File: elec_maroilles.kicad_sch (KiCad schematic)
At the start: 14 parts

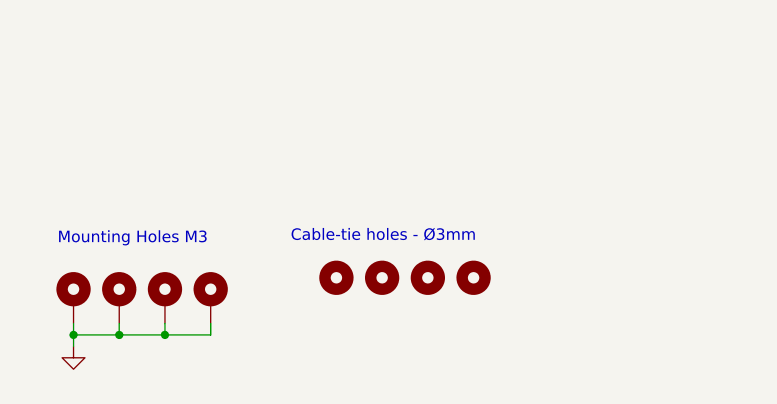
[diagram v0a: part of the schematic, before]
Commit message: [update] Better positionning.
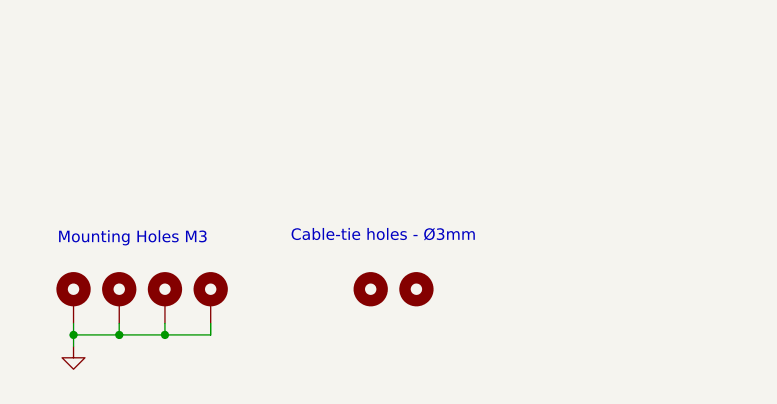
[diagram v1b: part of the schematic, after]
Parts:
- removed H12, H13: MountingHole_Pad, MountingHole:MountingHole_3.2mm_M3, symbol Mechanical:MountingHole
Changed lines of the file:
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@@
-	)
-	(symbol
-		(lib_id "Mechanical:MountingHole")
-		(at 146.05 170.18 0)
-		(unit 1)
-		(exclude_from_sim no)
-		(in_bom no)
-		(on_board yes)
-		(dnp no)
-		(property "Reference" "H13"
-			(at 148.59 168.91 0)
-			(effects
-				(font
-					(size 1.27 1.27)
-				)
-				(justify left)
-				(hide yes)
-			)
-		)
-		(property "Value" "MountingHole_Pad"
-			(at 152.4 163.83 0)
-			(effects
-				(font
-					(size 1.27 1.27)
-				)
-				(justify left)
-				(hide yes)
-			)
-		)
-		(property "Footprint" "MountingHole:MountingHole_3.2mm_M3"
-			(at 146.05 170.18 0)
-			(effects
-				(font
-					(size 1.27 1.27)
-				)
-				(hide yes)
-			)
-		)
-		(property "Datasheet" "~"
-			(at 146.05 170.18 0)
-			(effects
-				(font
-					(size 1.27 1.27)
-				)
-				(hide yes)
-			)
-		)
-		(property "Description" "Mounting Hole without connection"
-			(at 146.05 170.18 0)
-			(effects
-				(font
-					(size 1.27 1.27)
-				)
-				(hide yes)
-			)
-		)
-		(instances
-			(project "elec_zuuu_up"
-				(path "/bc05f5da-608c-4912-90e4-36b13d989976"
-					(reference "H13")
-					(unit 1)
-				)
-			)
-		)
 	)
 	(symbol
@@
 	(symbol
 		(lib_id "Mechanical:MountingHole")
-		(at 135.89 170.18 0)
+		(at 139.7 171.45 0)
 		(unit 1)
 		(exclude_from_sim no)
@@
 		(dnp no)
 		(property "Reference" "H11"
-			(at 138.43 168.91 0)
+			(at 142.24 170.18 0)
 			(effects
 				(font
@@
 		)
 		(property "Value" "MountingHole_Pad"
-			(at 142.24 163.83 0)
+			(at 146.05 165.1 0)
 			(effects
 				(font
@@
 		)
 		(property "Footprint" "MountingHole:MountingHole_3.2mm_M3"
-			(at 135.89 170.18 0)
-			(effects
-				(font
-					(size 1.27 1.27)
-				)
-				(hide yes)
-			)
-		)
-		(property "Datasheet" "~"
-			(at 135.89 170.18 0)
+			(at 139.7 171.45 0)
+			(effects
+				(font
+					(size 1.27 1.27)
+				)
+				(hide yes)
+			)
+		)
+		(property "Datasheet" "~"
+			(at 139.7 171.45 0)
 			(effects
 				(font
@@
 		)
 		(property "Description" "Mounting Hole without connection"
-			(at 135.89 170.18 0)
+			(at 139.7 171.45 0)
 			(effects
 				(font
@@
 				(path "/bc05f5da-608c-4912-90e4-36b13d989976"
 					(reference "FID1")
-					(unit 1)
-				)
-			)
-		)
-	)
-	(symbol
-		(lib_id "Mechanical:MountingHole")
-		(at 140.97 170.18 0)
-		(unit 1)
-		(exclude_from_sim no)
-		(in_bom no)
-		(on_board yes)
-		(dnp no)
-		(property "Reference" "H12"
-			(at 143.51 168.91 0)
-			(effects
-				(font
-					(size 1.27 1.27)
-				)
-				(justify left)
-				(hide yes)
-			)
-		)
-		(property "Value" "MountingHole_Pad"
-			(at 147.32 163.83 0)
-			(effects
-				(font
-					(size 1.27 1.27)
-				)
-				(justify left)
-				(hide yes)
-			)
-		)
-		(property "Footprint" "MountingHole:MountingHole_3.2mm_M3"
-			(at 140.97 170.18 0)
-			(effects
-				(font
-					(size 1.27 1.27)
-				)
-				(hide yes)
-			)
-		)
-		(property "Datasheet" "~"
-			(at 140.97 170.18 0)
-			(effects
-				(font
-					(size 1.27 1.27)
-				)
-				(hide yes)
-			)
-		)
-		(property "Description" "Mounting Hole without connection"
-			(at 140.97 170.18 0)
-			(effects
-				(font
-					(size 1.27 1.27)
-				)
-				(hide yes)
-			)
-		)
-		(instances
-			(project "elec_zuuu_up"
-				(path "/bc05f5da-608c-4912-90e4-36b13d989976"
-					(reference "H12")
 					(unit 1)
 				)
@@
 	(symbol
 		(lib_id "Mechanical:MountingHole")
-		(at 130.81 170.18 0)
+		(at 134.62 171.45 0)
 		(unit 1)
 		(exclude_from_sim no)
@@
 		(dnp no)
 		(property "Reference" "H10"
-			(at 133.35 168.91 0)
+			(at 137.16 170.18 0)
 			(effects
 				(font
@@
 		)
 		(property "Value" "MountingHole_Pad"
-			(at 137.16 163.83 0)
+			(at 140.97 165.1 0)
 			(effects
 				(font
@@
 		)
 		(property "Footprint" "MountingHole:MountingHole_3.2mm_M3"
-			(at 130.81 170.18 0)
-			(effects
-				(font
-					(size 1.27 1.27)
-				)
-				(hide yes)
-			)
-		)
-		(property "Datasheet" "~"
-			(at 130.81 170.18 0)
+			(at 134.62 171.45 0)
+			(effects
+				(font
+					(size 1.27 1.27)
+				)
+				(hide yes)
+			)
+		)
+		(property "Datasheet" "~"
+			(at 134.62 171.45 0)
 			(effects
 				(font
@@
 		)
 		(property "Description" "Mounting Hole without connection"
-			(at 130.81 170.18 0)
-			(effects
-				(font
+			(at 134.62 171.45 0)
+			(effects
+				(font

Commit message: [update] Release A1 -> in production at JLCPCB qtty 5
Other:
- note added: "02/12/2025"
- note removed: "xx/yy/2025"

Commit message: [error] To be fixed: inverted diff pairs on grippers pico5.
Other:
- note added: "Todo: - attention les paires 2/3 et 4/5 sont inversées sur les pico5 des grippers (cf. le câble du bras)."
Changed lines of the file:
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@@
+		)
+	)
+	(text "Todo:\n - attention les paires 2/3 et 4/5 sont inversées sur les \n    pico5 des grippers (cf. le câble du bras)."
+		(exclude_from_sim no)
+		(at 37.084 92.71 0)
+		(effects
+			(font
+				(size 2.0066 2.0066)
+			)
+			(justify left bottom)
 		)
 	)

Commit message: [update] Release B1!
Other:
- note added: "02/02/2026"
- note added: "B1"
- note added: "[fix] On gripper, USB and 485 twisted pairs where inverted."
- note removed: "Todo: - attention les paires 2/3 et 4/5 sont inversées sur les pico5 des grippers (cf. le câble du bras)."
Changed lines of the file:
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@@
 	(title_block
 		(title "elec_maroilles")
-		(date "2025-12-02")
-		(rev "A1")
+		(date "2026-02-02")
+		(rev "B1")
 		(company "Pollen Robotics / Hugging Face")
 	)
@@
 		)
 	)
+	(text "SN"
+		(exclude_from_sim no)
+		(at 78.994 50.8 0)
+		(effects
+			(font
+				(size 2.0066 2.0066)
+			)
+			(justify left bottom)
+		)
+	)
 	(text "A1"
 		(exclude_from_sim no)
 		(at 19.05 44.45 0)
+		(effects
+			(font
+				(size 2.0066 2.0066)
+			)
+			(justify left bottom)
+		)
+	)
+	(text "B1"
+		(exclude_from_sim no)
+		(at 19.304 50.8 0)
 		(effects
 			(font
@@
 		)
 	)
+	(text "[fix] On gripper, USB and 485 twisted pairs where inverted."
+		(exclude_from_sim no)
+		(at 92.964 50.8 0)
+		(effects
+			(font
+				(size 2.0066 2.0066)
+			)
+			(justify left bottom)
+		)
+	)
 	(text "\"elec_maroilles\" is USB 2.0 hub built with lockable USB connectors. It provides \nalso Dynamixel TTL and Dynamixel RS485 converters and the associated connectors \nfor Reachy 2's grippers and antennas."
 		(exclude_from_sim no)
 		(at 19.304 27.686 0)
+		(effects
+			(font
+				(size 2.0066 2.0066)
+			)
+			(justify left bottom)
+		)
+	)
+	(text "02/02/2026"
+		(exclude_from_sim no)
+		(at 39.624 50.8 0)
 		(effects
 			(font
@@
 		)
 	)
-	(text "Todo:\n - attention les paires 2/3 et 4/5 sont inversées sur les \n    pico5 des grippers (cf. le câble du bras)."
+	(text "EB"
 		(exclude_from_sim no)
-		(at 37.084 92.71 0)
+		(at 63.754 50.8 0)
 		(effects
 			(font
